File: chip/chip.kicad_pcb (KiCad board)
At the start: 4 copper layers, 8.4 x 7.6 mm, 2 parts, among them J1 DF40TC-30DP-0.4V(51), U1 HOME_VFBGA67_INTERFACE

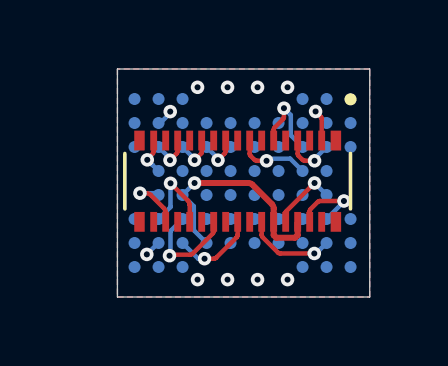
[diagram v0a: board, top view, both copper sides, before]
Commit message: Set board C geometry and nets, ready for routing
U1 to F.Cu, J1 to B.Cu concentric with it, C1/C2 to B.Cu in the strips
flanking the receptacle at +/-2.9 mm, clear of the outer 0.5 mm of both long
edges. Carrier A's 142 tracks stripped: every pad they terminated on has
changed side. Outline redrawn at 8.41 x 7.60 mm.

Two pcbnew traps worked around and documented in the script:

board.Remove() poisons the SWIG type registry. After the first removal,
GetFootprints(), GetTracks() and GetDrawings() all return bare SwigPyObjects
with no methods, so the script reads everything first, then removes, then
adds, then re-loads the saved file to report.

Edge.Cuts stroke width is 0.01 mm to match carrier A. The cut follows the
path centreline so this is cosmetic for fabrication, but the reported bounding
box is nominal plus stroke and both boards check against 8.42 x 7.61.

check_chip passes. J1's pad nets match the canonical DF40 table exactly and
the plug's MT lands are absent, confirming the receptacle.

Co-Authored-By: Claude Opus 5 <noreply@anthropic.com>
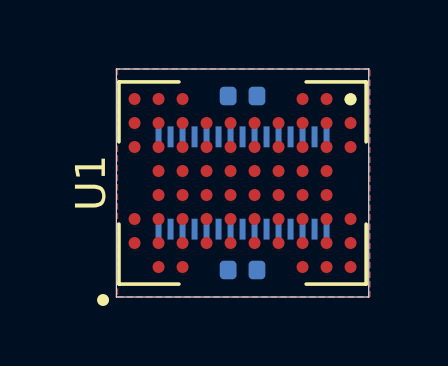
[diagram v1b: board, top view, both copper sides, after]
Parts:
- added C1: 100nF, Capacitor_SMD:C_0402_1005Metric, B.Cu at (168.5, 82.7)
- added C2: 1uF, Capacitor_SMD:C_0402_1005Metric, B.Cu at (168.5, 88.5)
- J1: value DF40TC-30DP-0.4V(51) -> DF40TC(4.0)-30DS-0.4V(51); footprint Connector_Hirose_DF40:HIROSE_DF40TC-30DP-0.4V_51_ -> Connector_Hirose_DF40:HIROSE_DF40TC_4.0_-30DS-0.4V_51_; moved to B.Cu
- U1: value HOME_VFBGA67_INTERFACE -> TC58NVG1S3HBAI6; footprint carrier:BGA-67_6.5x8.0mm_Layout8x10_P0.8mm_Mirrored_Interposer -> carrier:BGA-67_6.5x8.0mm_Layout8x10_P0.8mm; moved to F.Cu
- moved J1 0.17 mm to (168.5, 85.6), turned to 0 degrees
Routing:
- net VCC: track 7.72 -> 0.00 mm, vias 1 -> 0
- net /IO6: track 3.54 -> 0.00 mm, vias 1 -> 0
- net /RY//BY: track 3.02 -> 0.00 mm, vias 1 -> 0
- net /IO7: track 2.85 -> 0.00 mm, vias 1 -> 0
- net /IO8: track 2.83 -> 0.00 mm, vias 1 -> 0
- net //RE: track 2.76 -> 0.00 mm, vias 1 -> 0
- net /CLE: track 2.51 -> 0.00 mm, vias 1 -> 0
- net //WE: track 2.49 -> 0.00 mm, vias 1 -> 0
- net //CE: track 2.37 -> 0.00 mm, vias 1 -> 0
- net /IO5: track 2.11 -> 0.00 mm, vias 1 -> 0
- net /ALE: track 1.74 -> 0.00 mm, vias 1 -> 0
- net //WP: track 1.59 -> 0.00 mm, vias 1 -> 0
- net /IO3: track 1.35 -> 0.00 mm, vias 1 -> 0
- net /IO1: track 1.35 -> 0.00 mm, vias 1 -> 0
- net /IO2: track 1.35 -> 0.00 mm, vias 1 -> 0
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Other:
- outline, holes or cut-outs redrawn

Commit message: WIP: board C routing, 5 via-in-pad violations outstanding
All 22 nets now have copper and the GND pour is filled; DRC is down to one
unconnected item, an isolated island of the pour at (164.36, 88.79).

Not fabricable yet. check_chip fails: five vias sit inside BGA pads, which
the design forbids because it would require VIPPO rather than JLC's standard
4-layer flow.

  /CLE        ball C4   0.000 mm
  /IO4        ball J4   0.000 mm
  /IO5        ball J5   0.000 mm
  VCC         ball H5   0.001 mm
  /WP         ball B2   0.005 mm

Six vias also use a 0.25 mm drill rather than the 0.20 mm the other boards
use. Legal but inconsistent.

Snapshot of the on-disk file at 02:48 with KiCad still open, so any unsaved
edits are not included.

Co-Authored-By: Claude Opus 5 <noreply@anthropic.com>
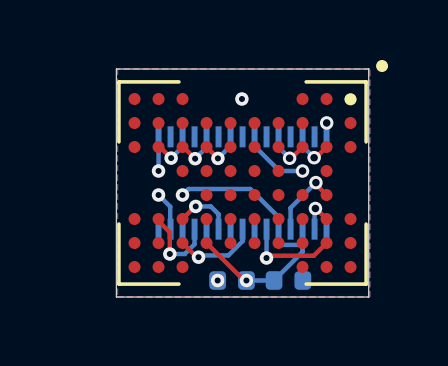
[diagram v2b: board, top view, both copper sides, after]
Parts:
- moved C1 6.34 mm to (170.1, 88.8)
- moved C2 0.49 mm to (168.2, 88.8), turned to 180 degrees
- turned U1 to -90 degrees
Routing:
- net VCC: track 0.00 -> 10.3 mm, vias 0 -> 2
- net /RY//BY: track 0.00 -> 3.17 mm, vias 0 -> 1
- net /IO8: track 0.00 -> 2.82 mm, vias 0 -> 1
- net /IO7: track 0.00 -> 2.78 mm, vias 0 -> 1
- net //CE: track 0.00 -> 2.46 mm, vias 0 -> 1
- net /CLE: track 0.00 -> 2.25 mm, vias 0 -> 1
- net /IO6: track 0.00 -> 1.98 mm, vias 0 -> 1
- net /IO2: track 0.00 -> 1.47 mm, vias 0 -> 1
- net //RE: track 0.00 -> 1.45 mm, vias 0 -> 1
- net /IO3: track 0.00 -> 1.44 mm, vias 0 -> 1
- net /IO1: track 0.00 -> 1.43 mm, vias 0 -> 1
- net /ALE: track 0.00 -> 1.42 mm, vias 0 -> 1
- net /IO5: track 0.00 -> 1.31 mm, vias 0 -> 1
- net //WE: track 0.00 -> 1.22 mm, vias 0 -> 1
- net /IO4: track 0.00 -> 1.14 mm, vias 0 -> 1
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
